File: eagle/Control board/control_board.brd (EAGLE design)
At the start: 160 x 100 mm, 54 parts

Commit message: Added battery and regulators. Added silks to nucleo footprint.
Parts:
- added C1, C2: 0.1u, rcl:C0603
- added IC1, IC2: (no value), custom:317TS
- added PAD1, PAD10, PAD2, PAD3, PAD4, PAD5, PAD6, PAD7, PAD8, PAD9: WIREPAD3,17/1,1, wirepad:3,17/1,1
- added R1, R2, R3, R4: (no value), rcl:R0603
- moved SB1 99.8 mm to (23.9, 34.0)
- moved SB17 99.8 mm to (23.9, 26.4)
- moved SB2 99.8 mm to (23.9, 31.5)
- moved SB32 99.8 mm to (23.9, 51.8)
- moved SB36 99.8 mm to (23.9, 64.5)
- moved SB41 99.8 mm to (23.9, 67.1)
- moved SB5 99.8 mm to (23.9, 29.0)
- moved SB51 99.8 mm to (23.9, 23.9)
- moved SB52 99.8 mm to (23.9, 21.3)
- moved SB53 99.8 mm to (23.9, 39.1)
- moved SB12 98.7 mm to (83.8, 51.8)
- moved SB13 98.7 mm to (83.8, 54.4)
- moved SB18 98.7 mm to (83.8, 39.1)
- moved SB19 98.7 mm to (83.8, 41.7)
- moved SB28 98.7 mm to (83.8, 49.3)
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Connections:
- new net N$1: IC2.1, R3.2, R4.1
- new net N$3: IC1.1, R1.2, R2.1
- new net PP12V: PAD1.1
- new net PP3V3: IC2.2, R3.1
- new net PP5V: IC1.2, R1.1
- new net PP8V: C1.1, C2.1, IC1.3, IC2.3, PAD5.1
- new net PPBATT: PAD4.1, PAD8.1, PAD9.1
- net GND: now also C1.2, C2.2, PAD10.1, PAD2.1, PAD3.1, PAD6.1, PAD7.1, R2.2, R4.2
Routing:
- net RESET_CONN: track 3.17 -> 8.51 mm
- net PP6V_CONN: track 3.17 -> 8.51 mm
- net PH1_CONN: track 3.17 -> 8.51 mm
- net PH0_CONN: track 3.17 -> 8.51 mm
- net PD2_CONN: track 3.17 -> 8.51 mm
- net PC3_CONN: track 3.17 -> 8.51 mm
- net PC2_CONN: track 3.17 -> 8.51 mm
- net PC1_CONN: track 3.17 -> 8.51 mm
- net PC15_CONN: track 3.17 -> 8.51 mm
- net PC14_CONN: track 3.17 -> 8.51 mm
- net PC13_CONN: track 3.17 -> 8.51 mm
- net PC12_CONN: track 3.17 -> 8.51 mm
- net PC11_CONN: track 3.17 -> 8.51 mm
- net PC10_CONN: track 3.17 -> 8.51 mm
- net PC0_CONN: track 3.17 -> 8.51 mm
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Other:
- board size 160 x 100 mm -> 100 x 100 mm

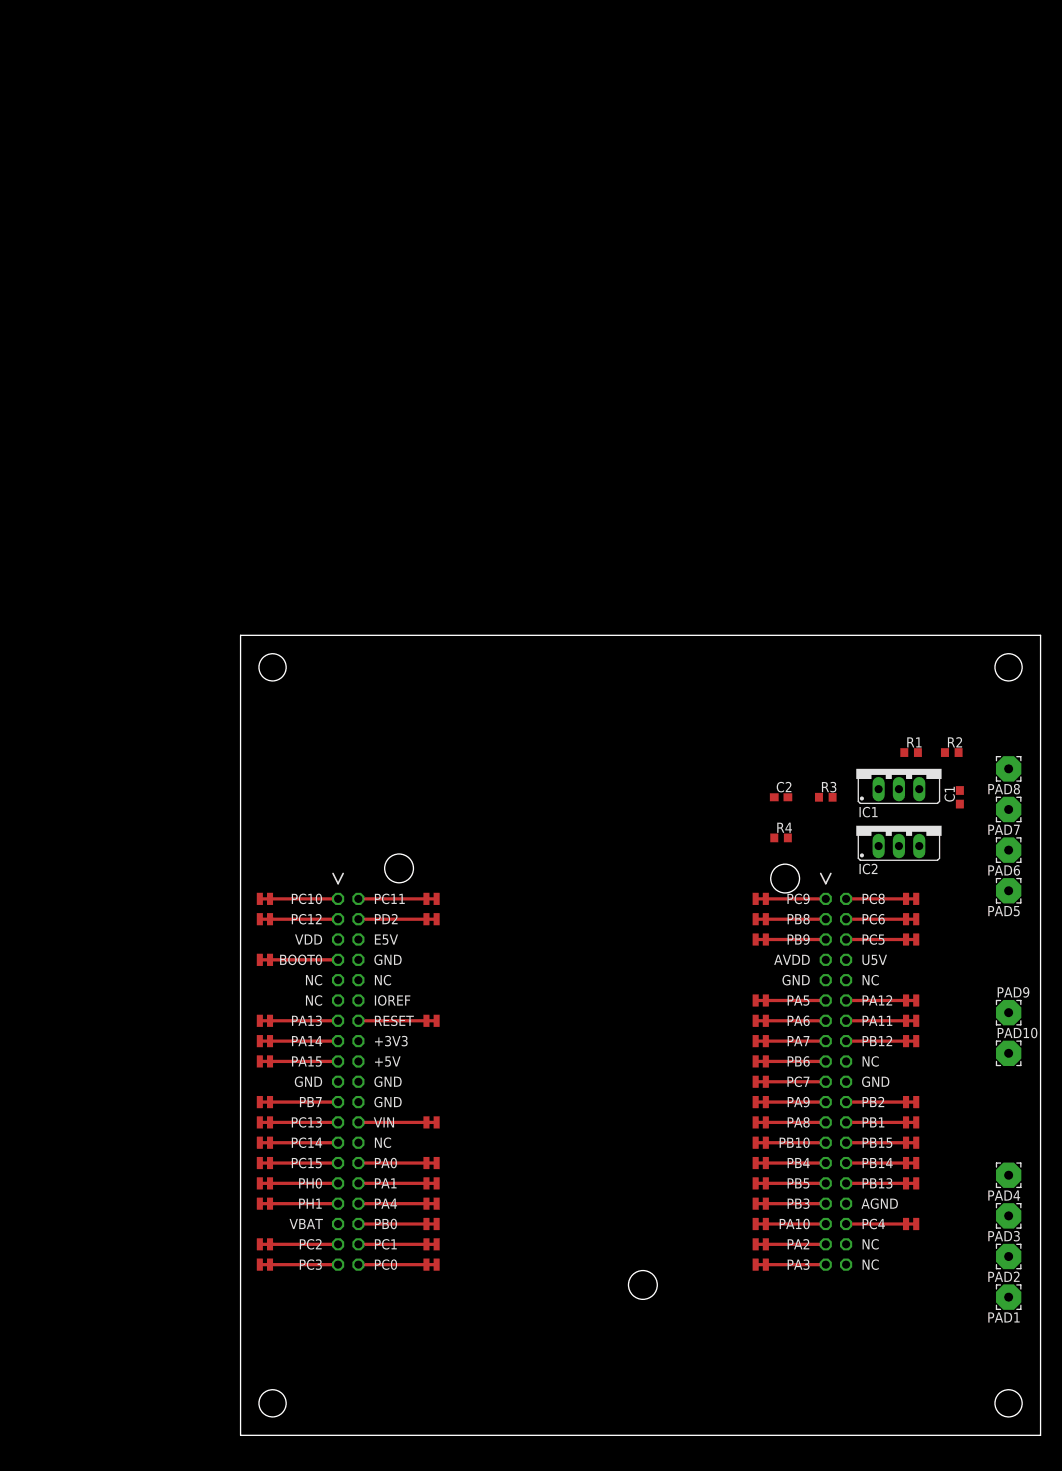
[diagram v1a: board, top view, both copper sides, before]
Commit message: Added connectors, more layout stuff
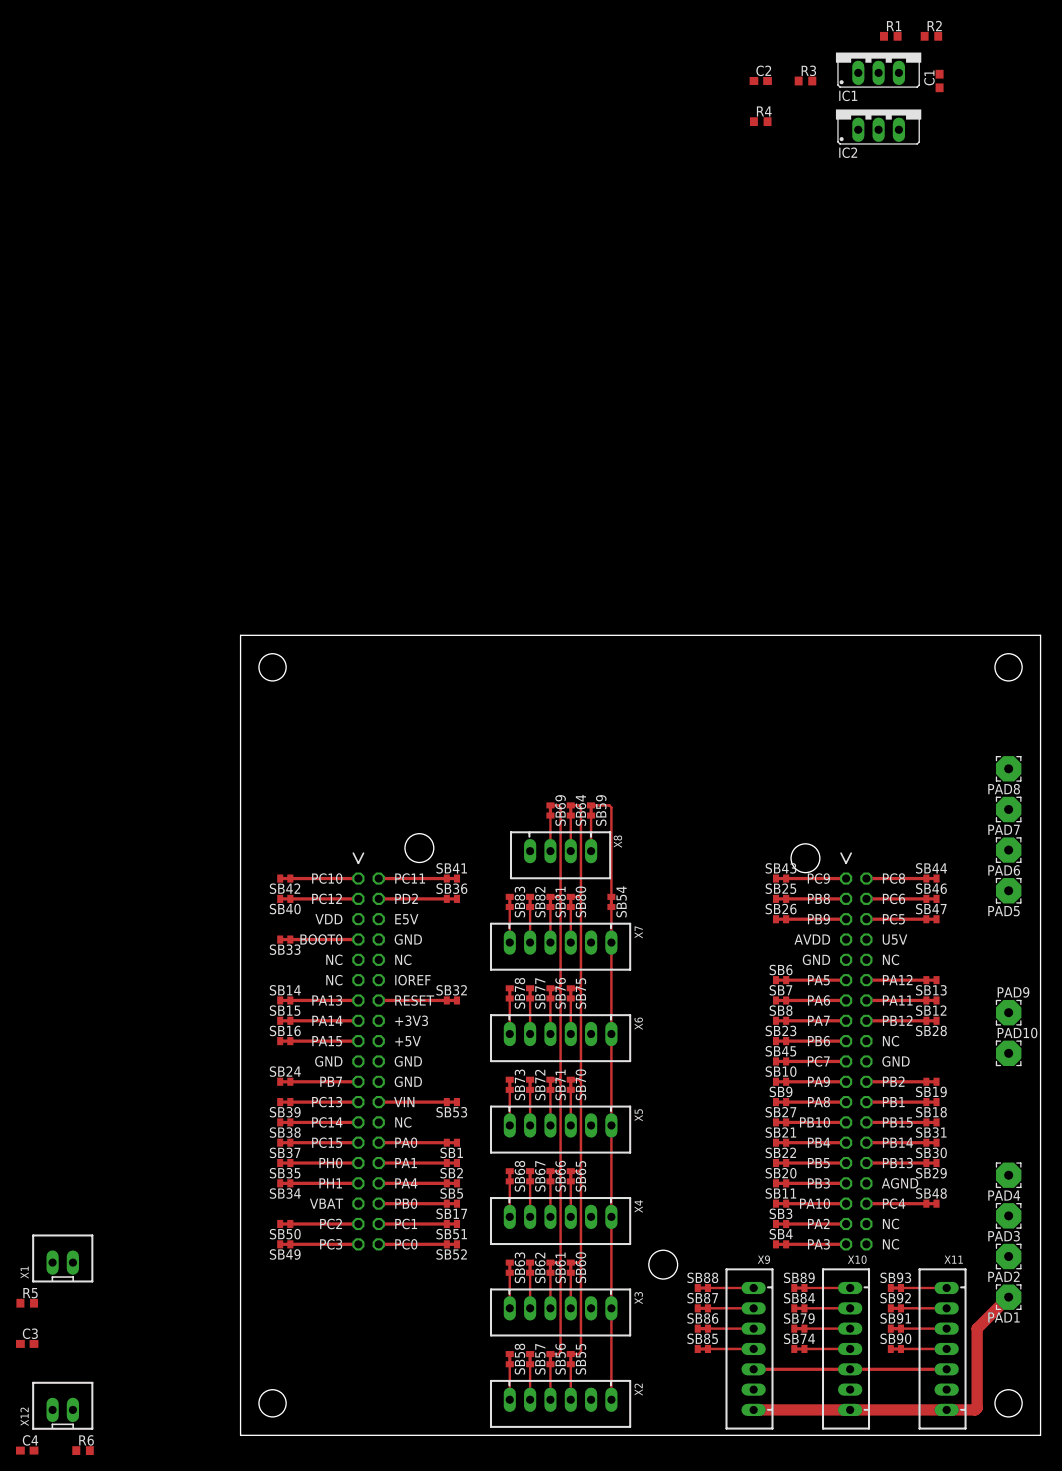
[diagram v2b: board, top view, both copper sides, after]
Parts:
- added C3, C4: 0.1uF, rcl:C0603
- added R5, R6: 1k, rcl:R0603
- added SB54, SB55, SB56, SB57, SB58, SB59, SB60, SB61, SB62, SB63, SB64, SB65, SB66, SB67, SB68, SB69, SB70, SB71, SB72, SB73, SB74, SB75, SB76, SB77, SB78, SB79, SB80, SB81, SB82, SB83, SB84, SB85, SB86, SB87, SB88, SB89, SB90, SB91, SB92, SB93: SOLDER_BRIDGE, custom:SOLDER_BRIDGE
- added X1, X12: JST-XH-02-PIN-LONG-PAD, con-jst-xh:JST-XH-02-PACKAGE-LONG-PAD
- added X10, X11, X9: JST-XH-07-PIN-LONG-PAD, con-jst-xh:JST-XH-07-PACKAGE-LONG-PAD
- added X2, X3, X4, X5, X6, X7: JST-XH-06-PIN-LONG-PAD, con-jst-xh:JST-XH-06-PACKAGE-LONG-PAD
- added X8: JST-XH-04-PIN-LONG-PAD, con-jst-xh:JST-XH-04-PACKAGE-LONG-PAD
- moved IC1 89.6 mm to (79.8, 172.8)
- moved IC2 89.6 mm to (79.8, 165.7)
- moved R4 89.6 mm to (65.0, 164.2)
- moved C1 89.6 mm to (87.4, 169.3)
- moved C2 89.6 mm to (65.0, 169.3)
- moved R1 89.6 mm to (81.3, 174.9)
- moved R2 89.6 mm to (86.4, 174.9)
- moved R3 89.6 mm to (70.6, 169.3)
- moved SB44 3.59 mm to (86.4, 69.6)
- moved SB47 3.59 mm to (86.4, 64.5)
- moved SB29 3.59 mm to (86.4, 34.0)
- moved SB16 3.59 mm to (5.59, 49.3)
- moved SB42 3.59 mm to (5.59, 69.6)
- moved SB12 3.59 mm to (86.4, 54.4)
- moved SB13 3.59 mm to (86.4, 56.9)
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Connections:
- net PP6V_CONN renamed PP8V_CONN
- new net IMU_SCL: SB64.P$2, X8.2
- new net IMU_SDA: SB69.P$2, X8.3
- new net IMU_VCC: SB59.P$2, X8.1
- new net M1_1: SB85.P$1
- new net M1_2: SB86.P$1
- new net M1_3: SB87.P$1
- new net M1_4: SB88.P$1
- new net M2_1: SB74.P$1
- new net M2_2: SB79.P$1
- new net M2_3: SB84.P$1
- new net M2_4: SB89.P$1
- new net M3_1: SB90.P$1
- new net M3_2: SB91.P$1
- new net M3_3: SB92.P$1
- new net M3_4: SB93.P$1
- new net MOTOR1_1EN: SB85.P$2, X9.4
- new net MOTOR1_2EN: SB86.P$2, X9.5
- new net MOTOR1_3EN: SB87.P$2, X9.6
- new net MOTOR1_4EN: SB88.P$2, X9.7
- new net MOTOR2_1EN: SB74.P$2, X10.4
- new net MOTOR2_2EN: SB79.P$2, X10.5
- new net MOTOR2_3EN: SB84.P$2, X10.6
- new net MOTOR2_4EN: SB89.P$2, X10.7
- new net MOTOR3_1EN: SB90.P$2, X11.4
- new net MOTOR3_2EN: SB91.P$2, X11.5
- new net MOTOR3_3EN: SB92.P$2, X11.6
- new net MOTOR3_4EN: SB93.P$2, X11.7
- new net RF1_G: SB57.P$1
- new net RF1_GPIO: SB57.P$2, X2.5
- new net RF1_SCL: SB55.P$2, X2.3
- new net RF1_SDA: SB56.P$2, X2.4
- new net RF1_X: SB58.P$1
- new net RF1_XSHUT: SB58.P$2, X2.6
- new net RF2_G: SB62.P$1
- new net RF2_GPIO: SB62.P$2, X3.5
- new net RF2_SCL: SB60.P$2, X3.3
- new net RF2_SDA: SB61.P$2, X3.4
- new net RF2_X: SB63.P$1
- new net RF2_XSHUT: SB63.P$2, X3.6
- new net RF3_G: SB67.P$1
- new net RF3_GPIO: SB67.P$2, X4.5
- new net RF3_SCL: SB65.P$2, X4.3
- new net RF3_SDA: SB66.P$2, X4.4
- new net RF3_X: SB68.P$1
- new net RF3_XSHUT: SB68.P$2, X4.6
- new net RF4_G: SB72.P$1
- new net RF4_GPIO: SB72.P$2, X5.5
- new net RF4_SCL: SB70.P$2, X5.3
- new net RF4_SDA: SB71.P$2, X5.4
- new net RF4_X: SB73.P$1
- new net RF4_XSHUT: SB73.P$2, X5.6
- new net RF5_G: SB77.P$1
- new net RF5_GPIO: SB77.P$2, X6.5
- new net RF5_SCL: SB75.P$2, X6.3
- new net RF5_SDA: SB76.P$2, X6.4
- new net RF5_X: SB78.P$1
- new net RF5_XSHUT: SB78.P$2, X6.6
- new net RF6_G: SB82.P$1
- new net RF6_GPIO: SB82.P$2, X7.5
- new net RF6_SCL: SB80.P$2, X7.3
- new net RF6_SDA: SB81.P$2, X7.4
- new net RF6_X: SB83.P$1
- new net RF6_XSHUT: SB83.P$2, X7.6
- new net RF_VCC: SB54.P$2, X2.1, X3.1, X4.1, X5.1, X6.1, X7.1
- new net SCL: SB55.P$1, SB60.P$1, SB64.P$1, SB65.P$1, SB70.P$1, SB75.P$1, SB80.P$1
- new net SDA: SB56.P$1, SB61.P$1, SB66.P$1, SB69.P$1, SB71.P$1, SB76.P$1, SB81.P$1
- new net SW1: C3.2, C4.2, R5.1, R6.1, X1.1, X12.1
- net GND: now also C3.1, C4.1, X1.2, X10.2, X11.2, X12.2, X2.2, X3.2, X4.2, X5.2, X6.2, X7.2, X8.4, X9.2
- net PC0_CONN: now also SB52.P$2; no longer SB52.P$1
- net PC1_CONN: now also SB51.P$2; no longer SB51.P$1
- net PC7_CONN: now also SB45.P$2; no longer SB45.P$1
- net PC9_CONN: now also SB43.P$2; no longer SB43.P$1
- net PP12V: now also X10.1, X11.1, X9.1
- net PP3V3: now also R5.2, R6.2, SB54.P$1, SB59.P$1
- net PP5V: now also X10.3, X11.3, X9.3
- net PP8V: now also SB53.P$1
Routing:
- net SDA: track 0.00 -> 77.0 mm
- net SCL: track 0.00 -> 77.0 mm
- net RF_VCC: track 0.00 -> 61.6 mm
- net PP12V: track 0.00 -> 43.5 mm
- net PP5V: track 0.00 -> 24.1 mm
- net PP3V3: track 0.00 -> 13.8 mm
- net MOTOR3_4EN: track 0.00 -> 5.72 mm
- net MOTOR3_3EN: track 0.00 -> 5.72 mm
- net MOTOR3_2EN: track 0.00 -> 5.72 mm
- net MOTOR3_1EN: track 0.00 -> 5.72 mm
- net MOTOR2_4EN: track 0.00 -> 5.72 mm
- net MOTOR2_3EN: track 0.00 -> 5.72 mm
- net MOTOR2_2EN: track 0.00 -> 5.72 mm
- net MOTOR2_1EN: track 0.00 -> 5.72 mm
- net MOTOR1_4EN: track 0.00 -> 5.72 mm
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
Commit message: Added more stuff
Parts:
- added LED1: (no value), adafruit:CHIPLED_0805
- added R7: 1k, rcl:R0603
- added SB100, SB101, SB102, SB103, SB104, SB105, SB106, SB108, SB109, SB110, SB111, SB112, SB113, SB114, SB115, SB94, SB95, SB96, SB97, SB98, SB99: SOLDER_BRIDGE, custom:SOLDER_BRIDGE
- added SW1: SPST_TACT-EVQQ2, adafruit:EVQ-Q2
- added X13, X14: JST-XH-03-PIN-LONG-PAD, con-jst-xh:JST-XH-03-PACKAGE-LONG-PAD
- added X15, X17: JST-XH-08-PIN-LONG-PAD, con-jst-xh:JST-XH-08-PACKAGE-LONG-PAD
- added X16, X18: JST-XH-02-PIN-LONG-PAD, con-jst-xh:JST-XH-02-PACKAGE-LONG-PAD
- moved C4 110.7 mm to (42.5, 84.5), turned to 90 degrees
- moved X12 108.7 mm to (43.8, 89.5)
- moved R6 108.0 mm to (45.1, 84.5), turned to 270 degrees
- moved C3 93.9 mm to (32.4, 84.5), turned to 90 degrees
- moved R5 91.7 mm to (34.9, 84.5), turned to 270 degrees
- moved X1 88.0 mm to (33.7, 89.5)
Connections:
- net PA13_CONN renamed TMS
- net PA14_CONN renamed TCK
- net PA2_CONN renamed USART2_TX
- net PA3_CONN renamed USART2_RX
- net PA5_CONN renamed BRD_LED
- net PB3_CONN renamed SWO
- net PC13_CONN renamed BRD_BUTTN
- net PP8V renamed PP7V
- new net IR1_1: SB5.P$1, SB99.P$1
- new net IR1_2: SB100.P$1, SB11.P$1
- new net IR1_3: SB101.P$1, SB12.P$1
- new net IR1_4: SB102.P$1, SB17.P$1
- new net IR1_5: SB103.P$1, SB18.P$1
- new net IR1_6: SB104.P$1, SB19.P$1
- new net IR1_7: SB105.P$1, SB21.P$1
- new net IR1_8: SB106.P$1, SB22.P$1
- new net IR1_IN1: SB99.P$2, X15.1
- new net IR1_IN2: SB100.P$2, X15.2
- new net IR1_IN3: SB101.P$2, X15.3
- new net IR1_IN4: SB102.P$2, X15.4
- new net IR1_IN5: SB103.P$2, X15.5
- new net IR1_IN6: SB104.P$2, X15.6
- new net IR1_IN7: SB105.P$2, X15.7
- new net IR1_IN8: SB106.P$2, X15.8
- new net IR2_1: SB108.P$1, SB28.P$1
- new net IR2_2: SB109.P$1, SB29.P$1
- new net IR2_3: SB110.P$1, SB30.P$1
- new net IR2_4: SB111.P$1, SB31.P$1
- new net IR2_5: SB112.P$1, SB52.P$1
- new net IR2_6: SB113.P$1, SB51.P$1
- new net IR2_7: SB114.P$1, SB50.P$2
- new net IR2_8: SB115.P$1, SB48.P$2
- new net IR2_IN1: SB108.P$2, X17.1
- new net IR2_IN2: SB109.P$2, X17.2
- new net IR2_IN3: SB110.P$2, X17.3
- new net IR2_IN4: SB111.P$2, X17.4
- new net IR2_IN5: SB112.P$2, X17.5
- new net IR2_IN6: SB113.P$2, X17.6
- new net IR2_IN7: SB114.P$2, X17.7
- new net IR2_IN8: SB115.P$2, X17.8
- new net IR_VCC: SB98.P$2, X16.1, X18.1
- new net N$2: SB7.P$1
- new net N$43: SB42.P$2
- new net N$44: SB41.P$2
- new net N$49: SB36.P$2
- new net N$50: SB35.P$2
- new net N$51: SB34.P$2
- new net RESET_BTN: SB32.P$2, SW1.A, SW1.A'
- new net SERVO1: SB1.P$1, SB95.P$1
- new net SERVO1_PWM: SB95.P$2, X13.2
- new net SERVO1_VCC: SB94.P$2, X13.1
- new net SERVO2: SB2.P$1, SB97.P$1
- new net SERVO2_PWM: SB97.P$2, X14.2
- new net SERVO2_VCC: SB96.P$2, X14.1
- new net SW2: C4.2, R6.1, X12.1
- net GND: now also SW1.B, SW1.B', X13.3, X14.3, X16.2, X18.2
- net M1_1: now also SB23.P$1
- net M1_2: now also SB13.P$1
- net M1_3: now also SB26.P$1
- net M1_4: now also SB47.P$2
- net M2_1: now also SB24.P$1
- net M2_2: now also SB9.P$1
- net M2_3: now also SB25.P$1
- net M2_4: now also SB10.P$1
- net M3_1: now also SB46.P$2
- net M3_2: now also SB45.P$1
- net M3_3: now also SB44.P$2
- net M3_4: now also SB43.P$1
- net PP3V3: now also SB98.P$1
- net PP5V: now also SB94.P$1, SB96.P$1
- net RF1_G: now also SB8.P$1
- net RF2_G: now also SB49.P$2
- net SCL: now also SB27.P$1
- net SDA: now also SB40.P$2
- net SW1: no longer C4.2, R6.1, X12.1
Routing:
- net SW2: track 0.00 -> 6.77 mm
- net SW1: track 0.00 -> 6.77 mm

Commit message: Added cube, gpio expander, rearranged gpios
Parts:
- added C5, C6, C7: 0.1uF, rcl:C0603
- added LED2, LED3, LED4: (no value), adafruit:CHIPLED_0805
- added R10, R8, R9: 82, rcl:R0603
- added R11, R12: 100, rcl:R0603
- added SB107, SB116, SB117, SB118, SB119, SB120: SOLDER_BRIDGE, custom:SOLDER_BRIDGE
- added SW2: SPST_TACT-EVQQ2, adafruit:EVQ-Q2
- added U1, U5, U6: TCA9554A, custom:SOIC16-1.27-10.2X7.5MM
- R5, R6: value 1k -> 4.7k
- R7: value 1k -> 430
- U2, U3: value (none) -> LM317
- U4: value NUCLEO -> STM32F446
- renumbered IC1 to U2, IC2 to U3, U$1 to U4
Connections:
- net PC14_CONN renamed OSC32_IN
- net PC15_CONN renamed OSC32_OUT
- net PH0_CONN renamed OSC_IN
- net PH1_CONN renamed OSC_OUT
- removed net N$2: SB7.P$1
- removed net N$44: SB41.P$2
- removed net N$49: SB36.P$2
- removed net N$50: SB35.P$2
- removed net N$51: SB34.P$2
- removed net SCL: SB27.P$1, SB55.P$1, SB60.P$1, SB64.P$1, SB65.P$1, SB70.P$1, SB75.P$1, SB80.P$1
- removed net SDA: SB40.P$2, SB56.P$1, SB61.P$1, SB66.P$1, SB69.P$1, SB71.P$1, SB76.P$1, SB81.P$1
- new net DBG_BUTTON: SB39.P$2, SW2.A, SW2.A'
- new net GPIOEXP1_SCL: SB116.P$2, U1.14
- new net GPIOEXP1_SDA: SB107.P$2, U1.15
- new net GPIOEXP2_SCL: SB118.P$2, U5.14
- new net GPIOEXP2_SDA: SB117.P$2, U5.15
- new net GPIOEXP3_P6: R9.1, U6.11
- new net GPIOEXP3_P7: R10.1, U6.12
- new net GPIOEXP3_SCL: SB120.P$2, U6.14
- new net GPIOEXP3_SDA: SB119.P$2, U6.15
- new net I2C2_SCL: SB116.P$1, SB118.P$1, SB120.P$1, SB27.P$1, SB55.P$1, SB60.P$1, SB64.P$1, SB65.P$1, SB70.P$1, SB75.P$1, SB80.P$1
- new net I2C2_SDA: SB107.P$1, SB117.P$1, SB119.P$1, SB40.P$2, SB56.P$1, SB61.P$1, SB66.P$1, SB69.P$1, SB71.P$1, SB76.P$1, SB81.P$1
- new net I2C3_SCL: SB9.P$1
- new net I2C3_SDA: SB21.P$1
- new net LED_3V3: LED2.A, R8.2
- new net LED_5V: LED1.A, R7.2
- new net LED_GPIOEXP3_P6: LED3.A, R9.2
- new net LED_GPIOEXP3_P7: LED4.A, R10.2
- new net N$4: SB43.P$1
- new net SW1_ILIM: C3.1, R11.2
- new net SW2_ILIM: C4.1, R12.2
- net GND: now also C5.1, C6.1, C7.1, LED1.C, LED2.C, LED3.C, LED4.C, R11.1, R12.1, SW2.B, SW2.B', U1.1, U1.2, U1.3, U1.8, U5.2, U5.3, U5.8, U6.1, U6.3, U6.8; no longer C3.1, C4.1
- net IR1_1: now also U1.4; no longer SB5.P$1
- net IR1_2: now also U1.5; no longer SB11.P$1
- net IR1_3: now also U1.6; no longer SB12.P$1
- net IR1_4: now also U1.7; no longer SB17.P$1
- net IR1_5: now also U1.9; no longer SB18.P$1
- net IR1_6: now also U1.10; no longer SB19.P$1
- net IR1_7: now also U1.11; no longer SB21.P$1
- net IR1_8: now also U1.12; no longer SB22.P$1
- net IR2_1: now also U5.4; no longer SB28.P$1
- net IR2_2: now also U5.5; no longer SB29.P$1
- net IR2_3: now also U5.6; no longer SB30.P$1
- net IR2_4: now also U5.7; no longer SB31.P$1
- net IR2_5: now also U5.9; no longer SB52.P$1
- net IR2_6: now also U5.10; no longer SB51.P$1
- net IR2_7: now also U5.11; no longer SB50.P$2
- net IR2_8: now also U5.12; no longer SB48.P$2
- net M1_2: no longer SB13.P$1
- net M1_3: now also SB24.P$1; no longer SB26.P$1
- net M1_4: no longer SB47.P$2
- net M2_1: now also SB25.P$1; no longer SB24.P$1
- net M2_2: now also SB11.P$1; no longer SB9.P$1
- net M2_3: now also SB26.P$1; no longer SB25.P$1
- net M2_4: now also SB22.P$1; no longer SB10.P$1
- net M3_1: now also SB7.P$1
- net M3_2: now also SB48.P$2; no longer SB45.P$1
- net M3_3: now also SB8.P$1
- net M3_4: now also SB29.P$1; no longer SB43.P$1
- net PP3V3: now also C5.2, C6.2, C7.2, R8.1, U1.16, U5.1, U5.16, U6.16, U6.2
- net PP5V: now also R7.1
- net RF1_G: now also SB52.P$1; no longer SB8.P$1
- net RF1_X: now also U6.4
- net RF2_G: now also SB51.P$1; no longer SB49.P$2
- net RF2_X: now also U6.5
- net RF3_G: now also SB17.P$1
- net RF3_X: now also U6.6
- net RF4_G: now also SB1.P$1
- net RF4_X: now also U6.7
- net RF5_G: now also SB36.P$2
- net RF5_X: now also U6.9
- net RF6_G: now also SB41.P$2
- net RF6_X: now also U6.10
- net SERVO1: now also SB30.P$1; no longer SB1.P$1
- net SERVO2: now also SB31.P$1; no longer SB2.P$1
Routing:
- net SDA: track 77.0 -> 0.00 mm
- net SCL: track 77.0 -> 0.00 mm
- net I2C2_SDA: track 0.00 -> 77.0 mm
- net I2C2_SCL: track 0.00 -> 77.0 mm
